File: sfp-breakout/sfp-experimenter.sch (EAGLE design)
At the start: 39 parts, among them IC1 TLV1117-25, IC2 SN65LVDS1DBV, IC3 SN65LVDT2DBV, J1 694108106102, X1 PINHD-1X4LOCK, X2 PINHD-1X4LOCK

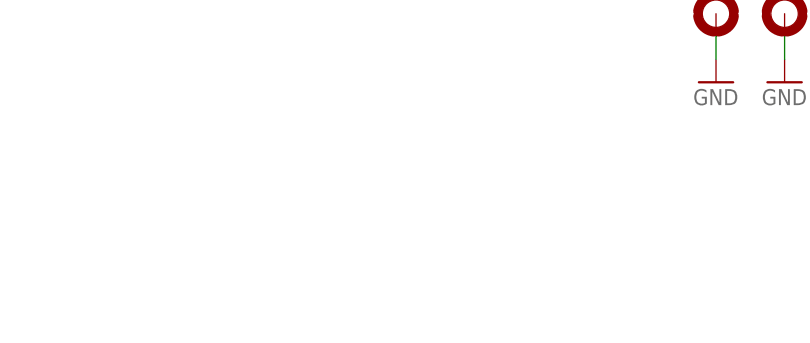
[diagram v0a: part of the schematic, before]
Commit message: sfp: add license to sch
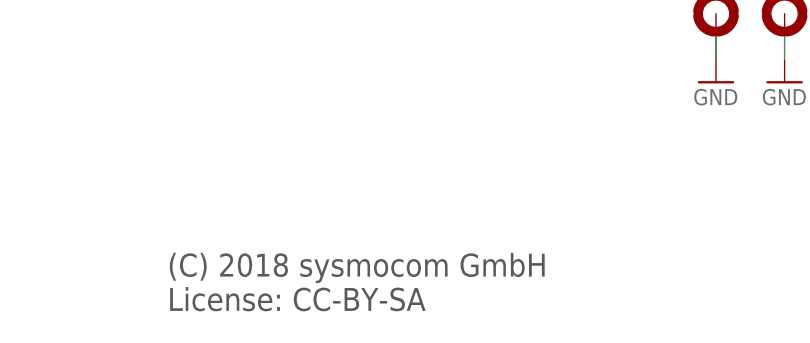
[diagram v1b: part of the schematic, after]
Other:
- note added: "(C) 2018 sysmocom GmbH License: CC-BY-SA"
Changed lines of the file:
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@@
 <plain>
 <text x="81.28" y="96.52" size="3.81" layer="97">3,3 V LDO</text>
+<text x="162.56" y="10.16" size="2.54" layer="97">(C) 2018 sysmocom GmbH
+License: CC-BY-SA</text>
 </plain>
 <instances>
@@
 </schematic>
 </drawing>
+<compatibility>
+<note version="6.3" minversion="6.2.2" severity="warning">
+Since Version 6.2.2 text objects can contain more than one line,
+which will not be processed correctly with this version.
+</note>
+</compatibility>
 </eagle>

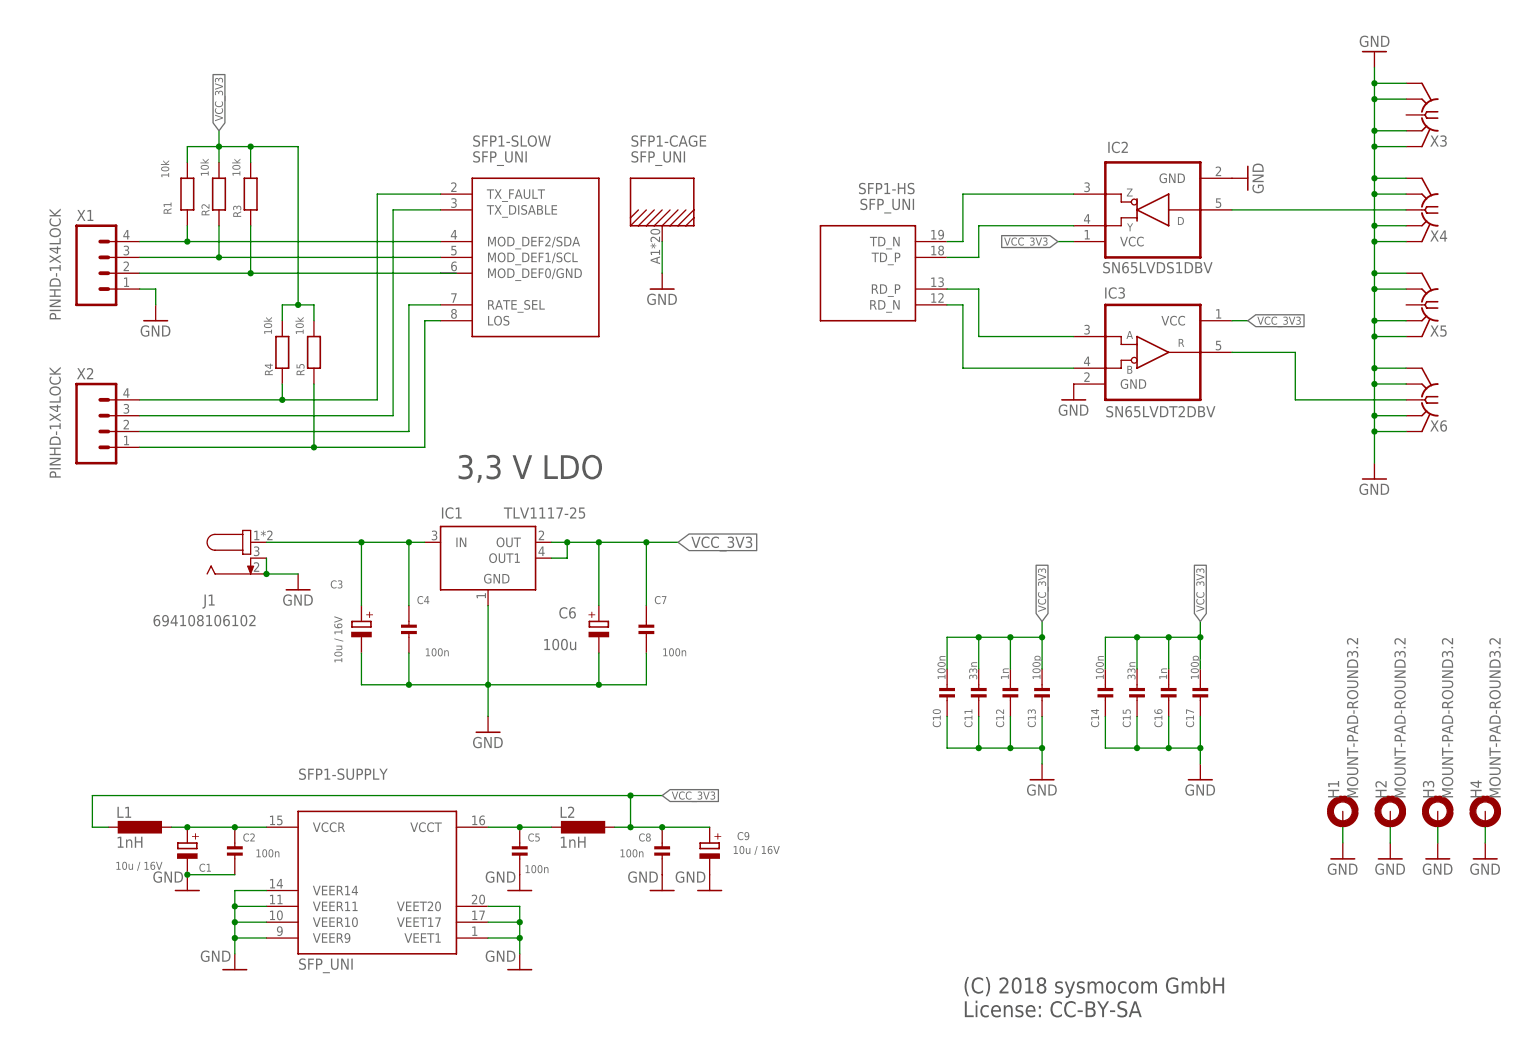
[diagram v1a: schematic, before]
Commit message: spf: revise both SFP designs (OSM#3313/OSM#3314)
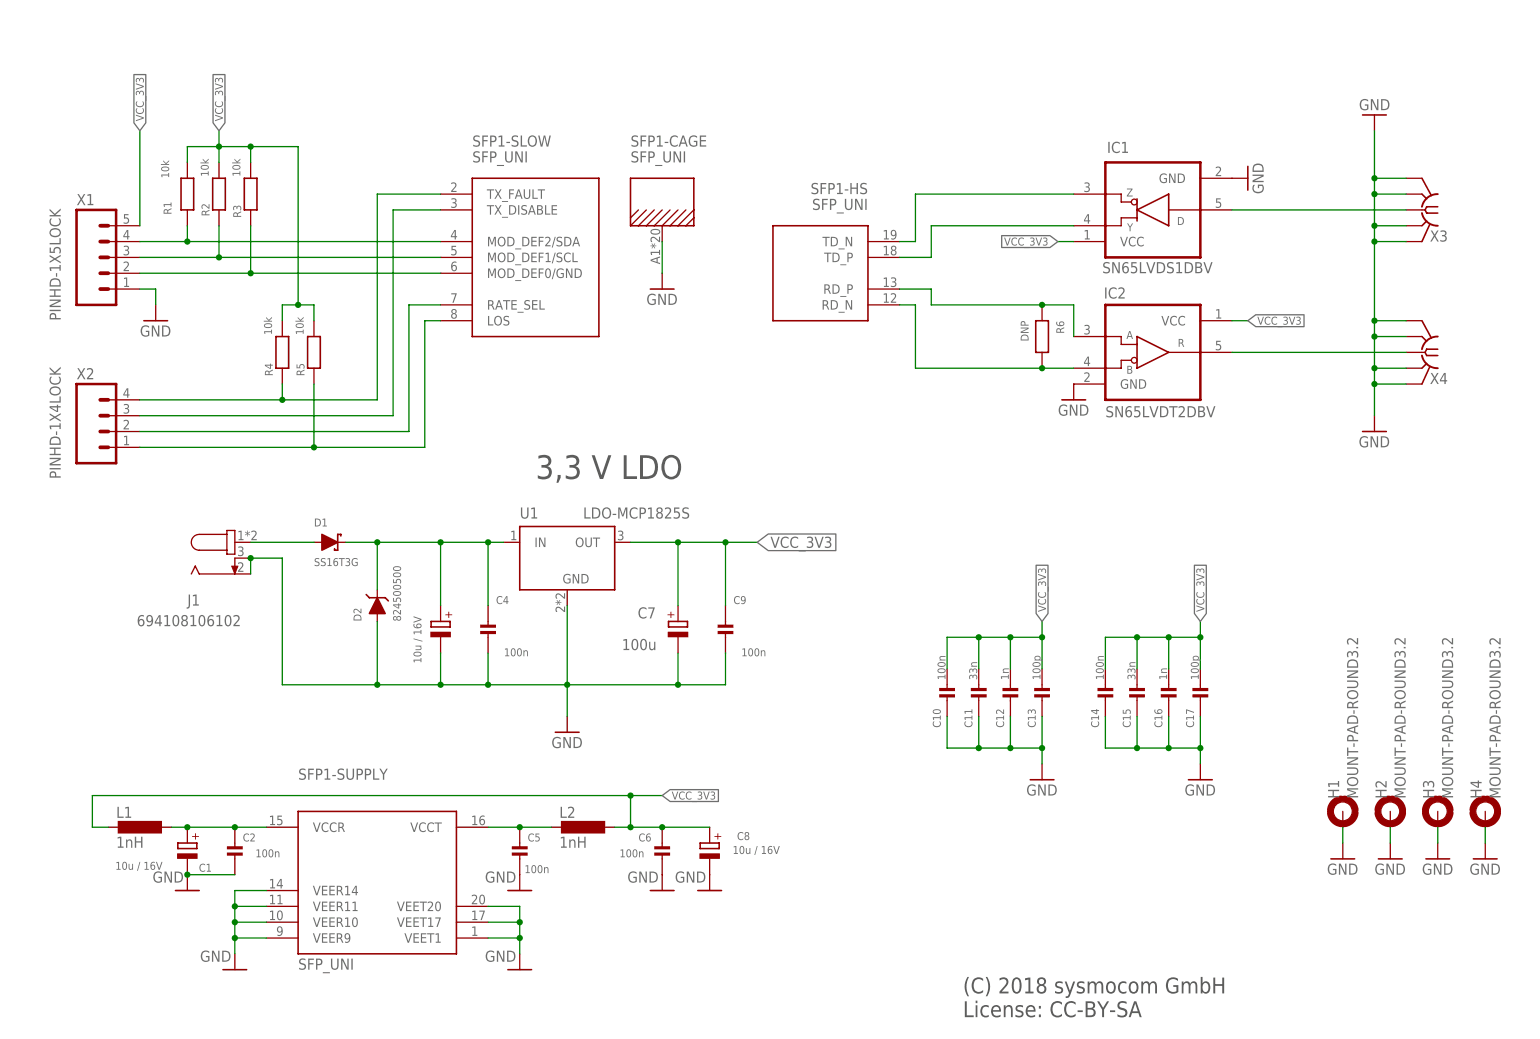
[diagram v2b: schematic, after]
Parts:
- removed IC3: SN65LVDT2DBV, sfp-experimenter:SN65LVDT2DBV
- removed X5, X6: (no value), sfp-experimenter:SMA-F-S-EDGE
- added D1: SS16T3G, sfp-experimenter:DIODE-SCHOTTKY-SMA
- added D2: 824500500, sfp-experimenter:DIODE-TVS-SMA
- added R6: DNP, sfp-experimenter:RESISTOR_0402
- added U1: LDO-MCP1825S, sfp-experimenter:LDO-MCP1825S
- C11, C12, C13, C15, C16, C17: CLASS (none) -> CAPACITOR; DESCRIPTION (none) -> NO DESCRIPTION; LINK (none) -> UNKNOWN LINK; MANUFACTURER (none) -> UNKNOWN MANUFACTURER; MANUFACTURERPARTNUMBER (none) -> UNKNOWN MANUFACTURER PART NUMBER; POPULATED (none) -> TRUE; ROHSCERTIFICATE (none) -> UNKNOWN ROHS CERTIFICATE; SOURCE (none) -> UNKNOWN SOURCE; SOURCEPARTNUMBER (none) -> UNKNOWN SOURCE PART NUMBER
- C6: value 100u -> 100n; device rcl:CPOL-EUCT6032 -> sfp-experimenter:CAP_CERAMIC_0603; DESCRIPTION CAP TANT 100UF 6.3V 10% 2413 -> CAP CER 0.1UF 16V X7R 0603; LINK http://www.digikey.de/product-detail/de/T491C107K006AT/399-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 -> http://www.digikey.de/product-detail/de/foo/1276-1005-1-ND; MANUFACTURER Kemet -> Samsung Electro-Mechanics; MANUFACTURERPARTNUMBER T491C107K006AT -> CL10B104KO8NNNC; ROHSCERTIFICATE Bleifrei / RoHS-konform -> UNKNOWN ROHS CERTIFICATE; SOURCEPARTNUMBER 399-8337-1-ND -> 1276-1005-1-ND
- C7: value 100n -> 100u; device sfp-experimenter:CAP_CERAMIC_0603 -> rcl:CPOL-EUCT6032; DESCRIPTION CAP CER 0.1UF 16V X7R 0603 -> CAP TANT 100UF 6.3V 10% 2413; LINK http://www.digikey.de/product-detail/de/foo/1276-1005-1-ND -> http://www.digikey.de/product-detail/de/T491C107K006AT/399-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; MANUFACTURER Samsung Electro-Mechanics -> Kemet; MANUFACTURERPARTNUMBER CL10B104KO8NNNC -> T491C107K006AT; ROHSCERTIFICATE UNKNOWN ROHS CERTIFICATE -> Bleifrei / RoHS-konform; SOURCEPARTNUMBER 1276-1005-1-ND -> 399-8337-1-ND
- C8: value 100n -> 10u / 16V; device sfp-experimenter:CAP_CERAMIC_0603 -> sfp-experimenter:CPOL-EU-1206; DESCRIPTION CAP CER 0.1UF 16V X7R 0603 -> CAP CER 10UF 16V X5R 0805; LINK http://www.digikey.de/product-detail/de/foo/1276-1005-1-ND -> https://www.digikey.de/product-detail/de/samsung-electro-me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; MANUFACTURERPARTNUMBER CL10B104KO8NNNC -> CL21A106KOCLRNC; SOURCEPARTNUMBER 1276-1005-1-ND -> 1276-2399-1-ND
- C9: value 10u / 16V -> 100n; device sfp-experimenter:CPOL-EU-1206 -> sfp-experimenter:CAP_CERAMIC_0603; DESCRIPTION CAP CER 10UF 16V X5R 0805 -> CAP CER 0.1UF 16V X7R 0603; LINK https://www.digikey.de/product-detail/de/samsung-electro-me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 -> http://www.digikey.de/product-detail/de/foo/1276-1005-1-ND; MANUFACTURERPARTNUMBER CL21A106KOCLRNC -> CL10B104KO8NNNC; SOURCEPARTNUMBER 1276-2399-1-ND -> 1276-1005-1-ND
- IC1: value TLV1117-25 -> SN65LVDS1DBV; device sfp-experimenter:TLV1117 -> sfp-experimenter:SN65LVDS1DBV; DESCRIPTION IC REG LIN 3.3V 800MA SOT223-4 -> NO DESCRIPTION; LINK https://www.digikey.de/product-detail/de/texas-instruments/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 -> UNKNOWN LINK; MANUFACTURER Texas Instruments -> UNKNOWN MANUFACTURER; MANUFACTURERPARTNUMBER TLV1117-33CDCYR -> UNKNOWN MANUFACTURER PART NUMBER; SOURCE DIGIKEY -> UNKNOWN SOURCE; SOURCEPARTNUMBER 296-21112-1-ND -> UNKNOWN SOURCE PART NUMBER
- IC2: value SN65LVDS1DBV -> SN65LVDT2DBV; device sfp-experimenter:SN65LVDS1DBV -> sfp-experimenter:SN65LVDT2DBV
- X1: value PINHD-1X4LOCK -> PINHD-1X5LOCK; device sfp-experimenter:PINHD-1X4LOCK -> sfp-experimenter:PINHD-1X5LOCK
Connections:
- removed net +VIN: C3.+, C4.1, IC1.IN, J1.1
- removed net N$2: IC3.R, X6.1
- removed net N$3: IC2.D, X4.1
- new net +VIN1: C3.+, C4.1, D1.C, D2.C, U1.IN
- new net N$1: D1.A, J1.1
- new net RD: IC2.R, X4.1
- new net TD: IC1.D, X3.1
- net GND: now also C6.2, C7.-, C8.-, C9.2, D2.A, U1.GND; no longer C6.-, C7.2, C8.2, C9.-, IC3.GND, X5.GND@1, X5.GND@2, X5.GND@3, X5.GND@4, X6.GND@1, X6.GND@2, X6.GND@3, X6.GND@4
- net RD_N: now also IC2.B, R6.2; no longer IC3.B
- net RD_P: now also IC2.A, R6.1; no longer IC3.A
- net TD_N: now also IC1.Z; no longer IC2.Z
- net TD_P: now also IC1.Y; no longer IC2.Y
- net VCC_3V3: now also C6.1, C7.+, C8.+, C9.1, IC1.VCC, U1.OUT, X1.5; no longer C6.+, C7.1, C8.1, C9.+, IC1.OUT, IC1.OUT1, IC3.VCC
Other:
- moved on the sheet: C4, J1, SFP1-HS, X3, X4

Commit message: sfp: add LOS, TX_FAULT LEDs + add more supply pinheader on both PCBs
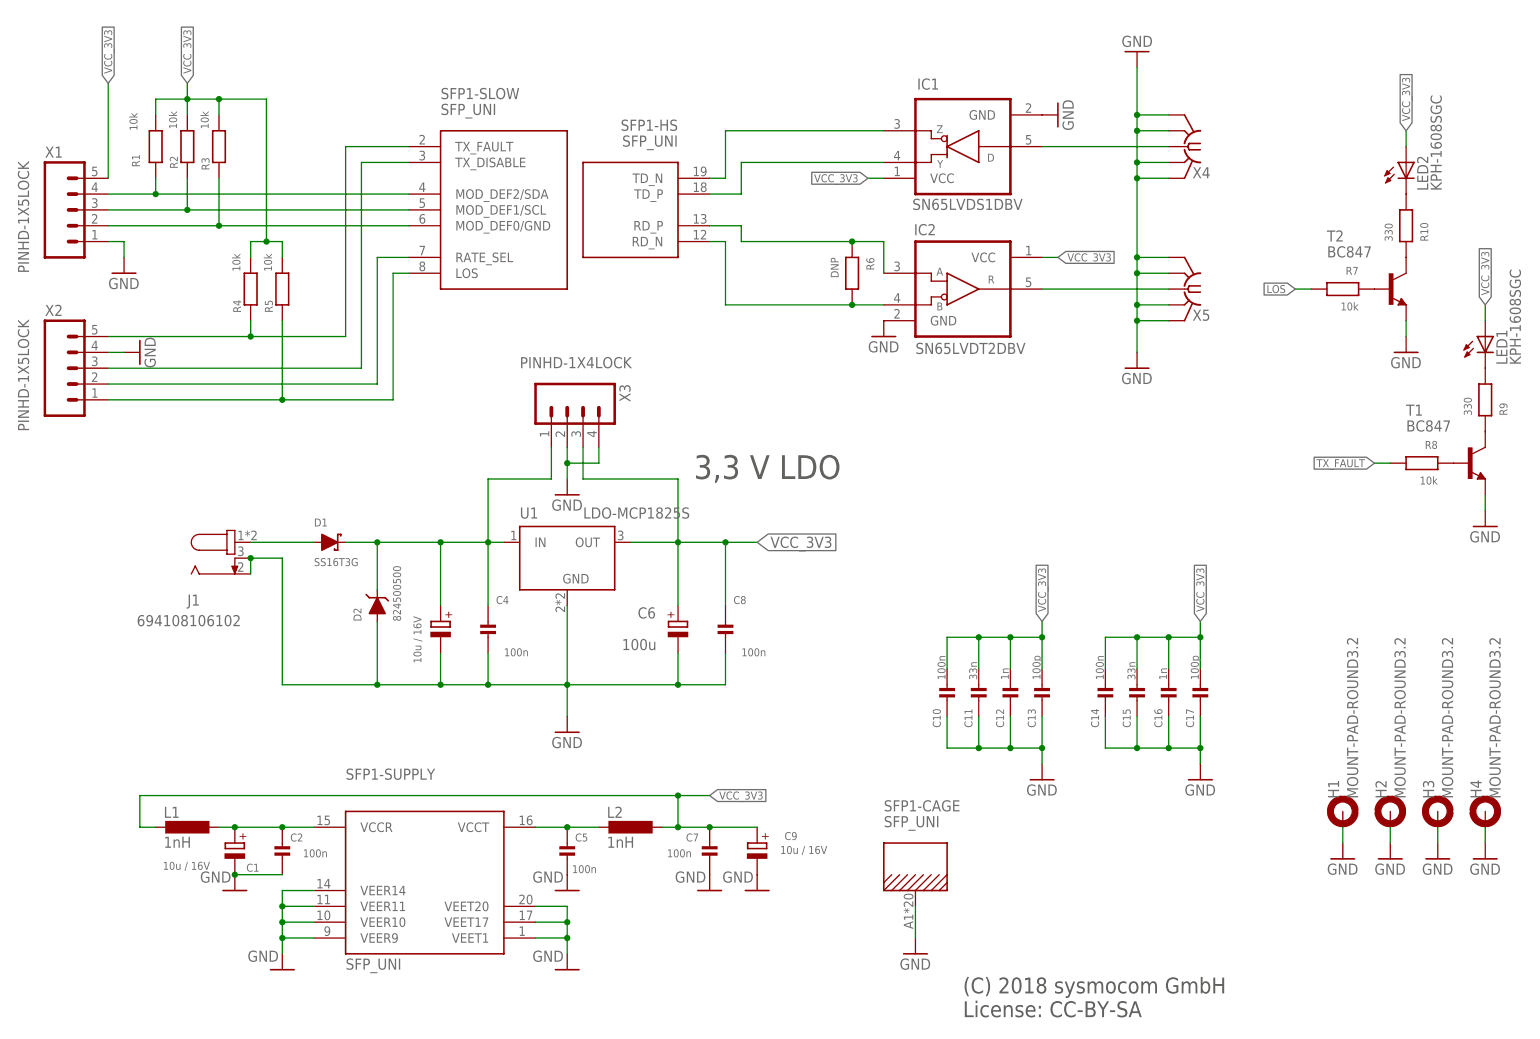
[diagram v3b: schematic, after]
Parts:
- added LED1, LED2: KPH-1608SGC, led:LEDCHIP-LED0603
- added R10, R9: 330, rc-sysmocom:RESISTOR_0603
- added R7, R8: 10k, rc-sysmocom:RESISTOR_0603
- added T1, T2: BC847, transistor:BC847C-NPN-SOT23-BEC
- added X5: (no value), sfp-experimenter:SMA-F-S-EDGE
- C6: value 100n -> 100u; device sfp-experimenter:CAP_CERAMIC_0603 -> rcl:CPOL-EUCT6032; DESCRIPTION CAP CER 0.1UF 16V X7R 0603 -> CAP TANT 100UF 6.3V 10% 2413; LINK http://www.digikey.de/product-detail/de/foo/1276-1005-1-ND -> http://www.digikey.de/product-detail/de/T491C107K006AT/399-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; MANUFACTURER Samsung Electro-Mechanics -> Kemet; MANUFACTURERPARTNUMBER CL10B104KO8NNNC -> T491C107K006AT; ROHSCERTIFICATE UNKNOWN ROHS CERTIFICATE -> Bleifrei / RoHS-konform; SOURCEPARTNUMBER 1276-1005-1-ND -> 399-8337-1-ND
- C7: value 100u -> 100n; device rcl:CPOL-EUCT6032 -> sfp-experimenter:CAP_CERAMIC_0603; DESCRIPTION CAP TANT 100UF 6.3V 10% 2413 -> CAP CER 0.1UF 16V X7R 0603; LINK http://www.digikey.de/product-detail/de/T491C107K006AT/399-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 -> http://www.digikey.de/product-detail/de/foo/1276-1005-1-ND; MANUFACTURER Kemet -> Samsung Electro-Mechanics; MANUFACTURERPARTNUMBER T491C107K006AT -> CL10B104KO8NNNC; ROHSCERTIFICATE Bleifrei / RoHS-konform -> UNKNOWN ROHS CERTIFICATE; SOURCEPARTNUMBER 399-8337-1-ND -> 1276-1005-1-ND
- C8: value 10u / 16V -> 100n; device sfp-experimenter:CPOL-EU-1206 -> sfp-experimenter:CAP_CERAMIC_0603; DESCRIPTION CAP CER 10UF 16V X5R 0805 -> CAP CER 0.1UF 16V X7R 0603; LINK https://www.digikey.de/product-detail/de/samsung-electro-me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 -> http://www.digikey.de/product-detail/de/foo/1276-1005-1-ND; MANUFACTURERPARTNUMBER CL21A106KOCLRNC -> CL10B104KO8NNNC; SOURCEPARTNUMBER 1276-2399-1-ND -> 1276-1005-1-ND
- C9: value 100n -> 10u / 16V; device sfp-experimenter:CAP_CERAMIC_0603 -> sfp-experimenter:CPOL-EU-1206; DESCRIPTION CAP CER 0.1UF 16V X7R 0603 -> CAP CER 10UF 16V X5R 0805; LINK http://www.digikey.de/product-detail/de/foo/1276-1005-1-ND -> https://www.digikey.de/product-detail/de/samsung-electro-me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; MANUFACTURERPARTNUMBER CL10B104KO8NNNC -> CL21A106KOCLRNC; SOURCEPARTNUMBER 1276-1005-1-ND -> 1276-2399-1-ND
- X2: value PINHD-1X4LOCK -> PINHD-1X5LOCK; device sfp-experimenter:PINHD-1X4LOCK -> sfp-experimenter:PINHD-1X5LOCK
- X3: value (none) -> PINHD-1X4LOCK; device sfp-experimenter:SMA-F-S-EDGE -> sfp-experimenter:PINHD-1X4LOCK
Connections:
- new net N$138: R8.1, T1.B
- new net N$139: LED1.C, R9.2
- new net N$141: R9.1, T1.C
- new net N$3: R7.1, T2.B
- new net N$4: LED2.C, R10.2
- new net N$7: R10.1, T2.C
- net +VIN1: now also X3.1
- net GND: now also C6.-, C7.2, C8.2, C9.-, T1.E, T2.E, X2.4, X3.2, X3.4, X5.GND@1, X5.GND@2, X5.GND@3, X5.GND@4; no longer C6.2, C7.-, C8.-, C9.2, X3.GND@1, X3.GND@2, X3.GND@3, X3.GND@4
- net LOS: now also R7.2
- net RD: now also X5.1; no longer X4.1
- net TD: now also X4.1; no longer X3.1
- net TX_FAULT: now also R8.2, X2.5; no longer X2.4
- net VCC_3V3: now also C6.+, C7.1, C8.1, C9.+, LED1.A, LED2.A, X3.3; no longer C6.1, C7.+, C8.+, C9.1
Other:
- moved on the sheet: C1, C2, C5, IC1, IC2, L1, L2, R1, R2, R3, R4, R5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
